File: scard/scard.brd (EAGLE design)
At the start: 47 x 86.5 mm, 66 parts, among them Q1 FDN360P, X1 COAX, X2 1365-20

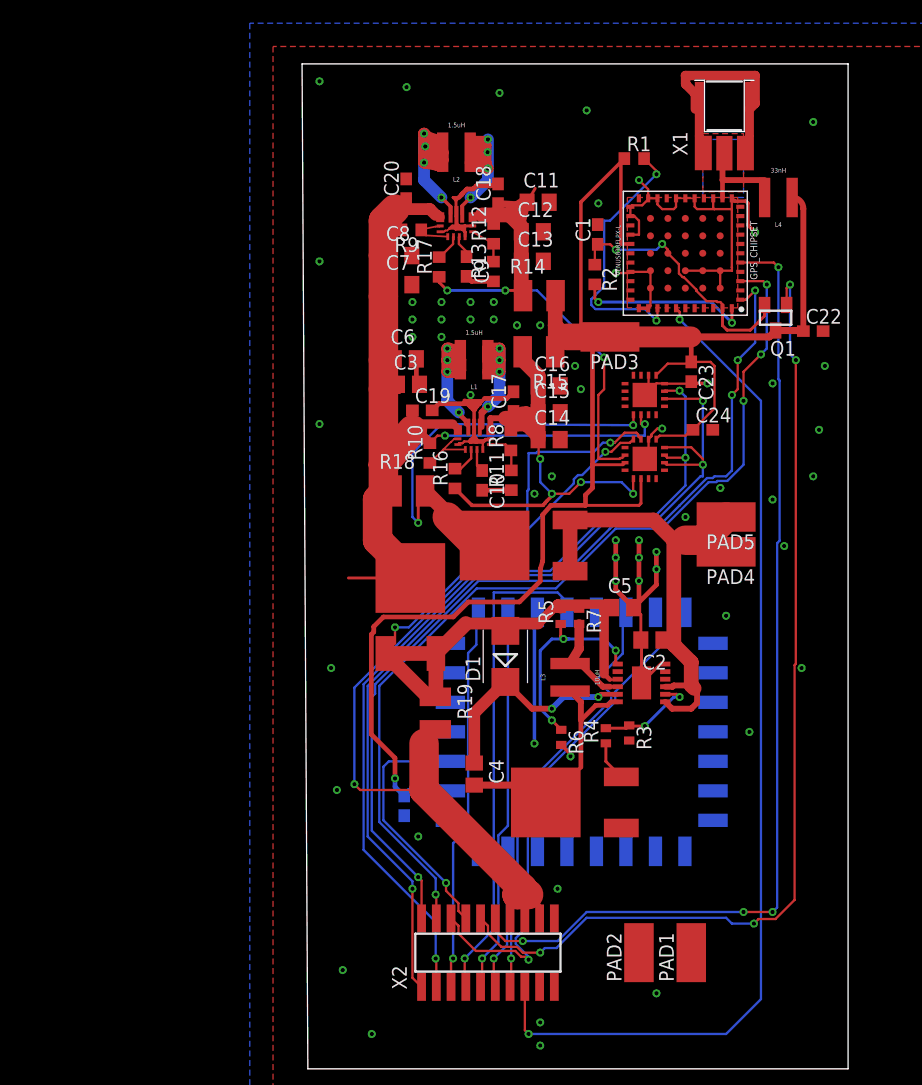
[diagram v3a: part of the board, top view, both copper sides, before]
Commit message: need switching voltage regulator capable of up to 8A
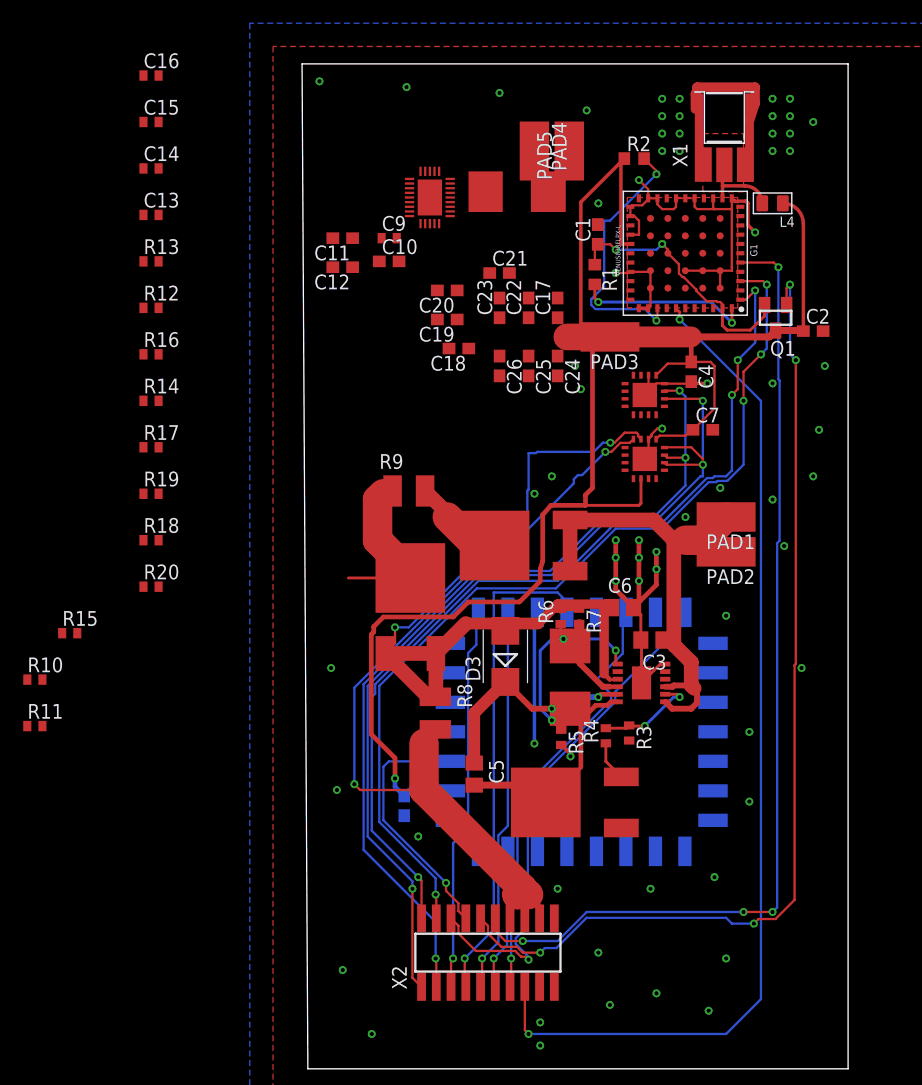
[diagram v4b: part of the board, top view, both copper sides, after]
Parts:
- removed L1: 1.5uH, calsat:XFL4020
- removed U$1: B085BM30, calsat:TO-252
- removed U$6, U$7: TPS63070, calsat:VQFN15
- added C25, C26: 10uF, resistor:C0603
- added D3: ES2D, diode:SMB
- added P1: TPS548A20, calsat:R-PWQFN-N28
- added R20: 3, rcl:R0402
- C10: value 100nF -> 10uF; device rcl:C0603 -> resistor:C0603
- C11, C12: value 22uF -> 10uF; device rcl:C0805 -> resistor:C0603
- C13: value 22uF -> 0.1uF; device rcl:C0805 -> resistor:C0402
- C14, C15: value 22uF -> 1uF; device rcl:C0805 -> resistor:C0402
- C16: value 22uF -> 470pF; device rcl:C0805 -> resistor:C0402
- C17, C18, C19, C20: value 10uF -> 22uF; device rcl:C0603 -> resistor:C0603
- C2: value 20uF -> 10uF; device resistor:C0805 -> resistor:C0603
- C21, C22: value 10uF -> 22uF
- C23, C24: value 0.1uF -> 10uF
- C3: value 10uF -> 20uF; device rcl:C0805 -> resistor:C0805
- C4: value 1uF -> 0.1uF; device resistor:C0805 -> resistor:C0603
- C5: value 10uF -> 1uF
- C6: device rcl:C0805 -> resistor:C0805
- C7: value 10uF -> 0.1uF; device rcl:C0805 -> resistor:C0603
- C8: device rcl:C0805 -> resistor:C0603
- C9: value 100nF -> 2.2nF; device rcl:C0603 -> resistor:C0402
- D1: value ES2D -> B085BM30; device diode:SMB -> calsat:TO-252
- L2: value 1.5uH -> 10uH; device calsat:XFL4020 -> calsat:SRP7028A
- L3: value 10uH -> 1.5uH; device calsat:XFL4020 -> calsat:SRP7028A
- L4: device calsat:XFL4020 -> Seeed-Inductor:L0805
- R1: value 1K -> 10K
- R10: value 10k -> 200k; device resistor:R0603 -> rcl:R0402
- R11: value 150k -> 200k; device resistor:R0603 -> rcl:R0402
- R12: value 470k -> 249k; device resistor:R0603 -> rcl:R0402
- R13: value 150k -> 105k; device resistor:R0603 -> rcl:R0402
- R14: value 0.01 -> 100k; device resistor:R1210 -> rcl:R0402
- R15: value 0.01 -> 0; device resistor:R1210 -> rcl:R0402
- R16: value 100k -> 150k; device resistor:R0603 -> rcl:R0402
- R17: value 100k -> 64.9k; device resistor:R0603 -> rcl:R0402
- R18: value 0.01 -> 9k; device resistor:R1210 -> rcl:R0402
- R19: value 0.01 -> 2k; device resistor:R1210 -> rcl:R0402
- R2: value 10K -> 1K
- R5: value ~630k -> ~410k
- R6: value ~410k -> ~630k
- R8: value 470k -> 0.01; device resistor:R0603 -> resistor:R1210
- R9: value 10k -> 0.01; device resistor:R0603 -> resistor:R1210
- moved C8 47.4 mm to (8.29, 22.6), flipped to the bottom, turned to 270 degrees
- moved R15 47.1 mm to (-20.5, 37.5), turned to 0 degrees
- moved C21 46.6 mm to (16.5, 68.5), flipped to the top, turned to 0 degrees
- moved L2 46.2 mm to (22.6, 33.7), turned to 90 degrees
- moved R11 46.1 mm to (-23.5, 29.5), turned to 0 degrees
- moved C16 43.5 mm to (-13.5, 85.5)
- moved C15 42.4 mm to (-13.5, 81.5)
- moved L3 42.0 mm to (18.0, 75.5), turned to 0 degrees
- moved C14 41.5 mm to (-13.5, 77.5)
- moved C4 39.3 mm to (33.0, 60.0)
- moved R10 39.2 mm to (-23.5, 33.5), turned to 0 degrees
- moved PAD4 38.2 mm to (19.5, 79.0), turned to 180 degrees
- moved PAD1 37.6 mm to (36.0, 47.5), turned to 90 degrees
- moved PAD2 35.3 mm to (36.0, 44.5), turned to 90 degrees
- moved R14 34.6 mm to (-13.5, 57.5)
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- renumbered A3 to A2, CHRG_IC to T1, GPS_CHIPSET to G1, U$2 to V1, U$4 to D4, U$5 to D2
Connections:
- net N$32 renamed SOLAR1_CUR
- net N$33 renamed VSOLAR1
- net N$34 renamed SOLAR2_CUR
- net N$35 renamed VSOLAR2
- removed net REG0_EN: R10.1, U$6.1, U$6.14
- removed net REG0_PGOOD: R16.2, U$6.2
- removed net REG1_3V3: A1.15, C11.1, C12.1, C13.1, C18.1, R12.2, R14.1, R17.1, U$7.7
- removed net REG1_EN: R9.1, U$7.1, U$7.14
- removed net REG1_PGOOD: R17.2, U$7.2
- removed net SYS_UNREG: A2.11, C19.1, C20.1, C3.1, C6.1, C7.1, C8.1, D4.1, R10.2, R18.1, R9.2, U$6.12, U$7.12
- new net N$1: P1.21, R16.1
- new net N$17: C16.1, R20.1
- new net N$2: C13.2, L3.1, P1.6, P1.7, P1.8, P1.9, R20.2
- new net SOLAR0_CUR: A2.12
- new net VSOLAR0: A2.11
- new net VSYS_UNREG: A1.14, C10.1, C11.1, C12.1, C14.1, C9.1, D4.1, P1.15, P1.16, P1.17, P1.19, R10.2, R9.1
- net +12V: now also C3.1, D1.2, D1.3, PAD1.1, PAD2.1; no longer C2.1, PAD4.1, PAD5.1, U$1.2, U$1.3
- net +3V3: now also C17.1, C18.1, C19.1, C2.1, C20.1, C25.1, C26.1, C4.1, C7.1, C8.1, L3.2, P1.24, R18.2, R2.1; no longer A1.14, R1.1, R14.2, R15.1
- net GND: now also C25.2, C26.2, C4.2, P1.10, P1.11, P1.12, P1.13, P1.14, P1.22, P1.27, P1.28, P1.29, PAD4.1, PAD5.1, R17.2, R19.1, R5.2; no longer C13.2, C5.2, PAD1.1, PAD2.1, R6.2, U$6.10, U$6.15, U$6.4, U$6.6, U$7.10, U$7.15, U$7.4, U$7.6
- net N$10: now also C15.1, P1.20, R12.2, R14.1; no longer R12.1, R13.2, U$7.5
- net N$11: now also P1.1, R12.1, R13.2; no longer L2.2, U$7.11
- net N$12: now also P1.2, R14.2, R16.2; no longer L2.1, U$7.9
- net N$13: now also P1.25, R17.1; no longer L1.1, U$6.9
- net N$14: now also P1.23, R18.1, R19.2; no longer R11.2, R8.1, U$6.5
- net N$15: now also P1.3, R10.1, R11.2; no longer L1.2, U$6.11
- net N$22: now also R1.1; no longer R2.1
- net N$3: now also C5.1, D3.C; no longer C4.1, D1.C
- net N$4: now also C5.2, L2.1; no longer C4.2, L3.1
- net N$5: now also P1.4, R15.1; no longer C9.1, U$7.3
- net N$6: now also L2.2; no longer L3.2
- net N$7: now also R2.2; no longer R1.2
- net N$8: now also R1.2; no longer R2.2
- net N$9: now also C13.1, R15.2; no longer C10.1, U$6.3
- net REG0_3V3: no longer C14.1, C15.1, C16.1, C17.1, R15.2, R16.1, R8.2, U$6.7
- net SYS_UNREG_CUR: now also A1.15, D1.1, R9.2; no longer A2.12, R18.2, U$1.1
- net VBATT: now also R8.2; no longer R19.2
- net VBATT_CUR: now also C6.1, D3.A, R6.2, R8.1; no longer C5.1, D1.A, R19.1, R5.2
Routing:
- net SYS_UNREG: track 86.0 -> 0.00 mm, vias 2 -> 0
- net REG1_3V3: track 52.2 -> 0.00 mm, vias 3 -> 0
- net REG0_3V3: track 50.1 -> 0.00 mm, vias 4 -> 0
- net GND: track 159.1 -> 118.0 mm, vias 60 -> 68
- net SYS_UNREG_CUR: track 38.2 -> 8.12 mm, vias 2 -> 0
- net N$11: track 26.0 -> 0.00 mm, vias 4 -> 0
- net N$12: track 21.3 -> 0.00 mm, vias 4 -> 0
- net VSYS_UNREG: track 0.00 -> 15.6 mm
- net N$15: track 14.9 -> 0.00 mm, vias 4 -> 0
- net N$13: track 13.6 -> 0.00 mm, vias 4 -> 0
- net +3V3: track 152.0 -> 142.7 mm
- net REG0_EN: track 5.17 -> 0.00 mm
- net REG1_EN: track 4.29 -> 0.00 mm
- net N$14: track 3.77 -> 0.00 mm
- net N$10: track 3.65 -> 0.00 mm
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- removed copper zone on layer 16, net NONE

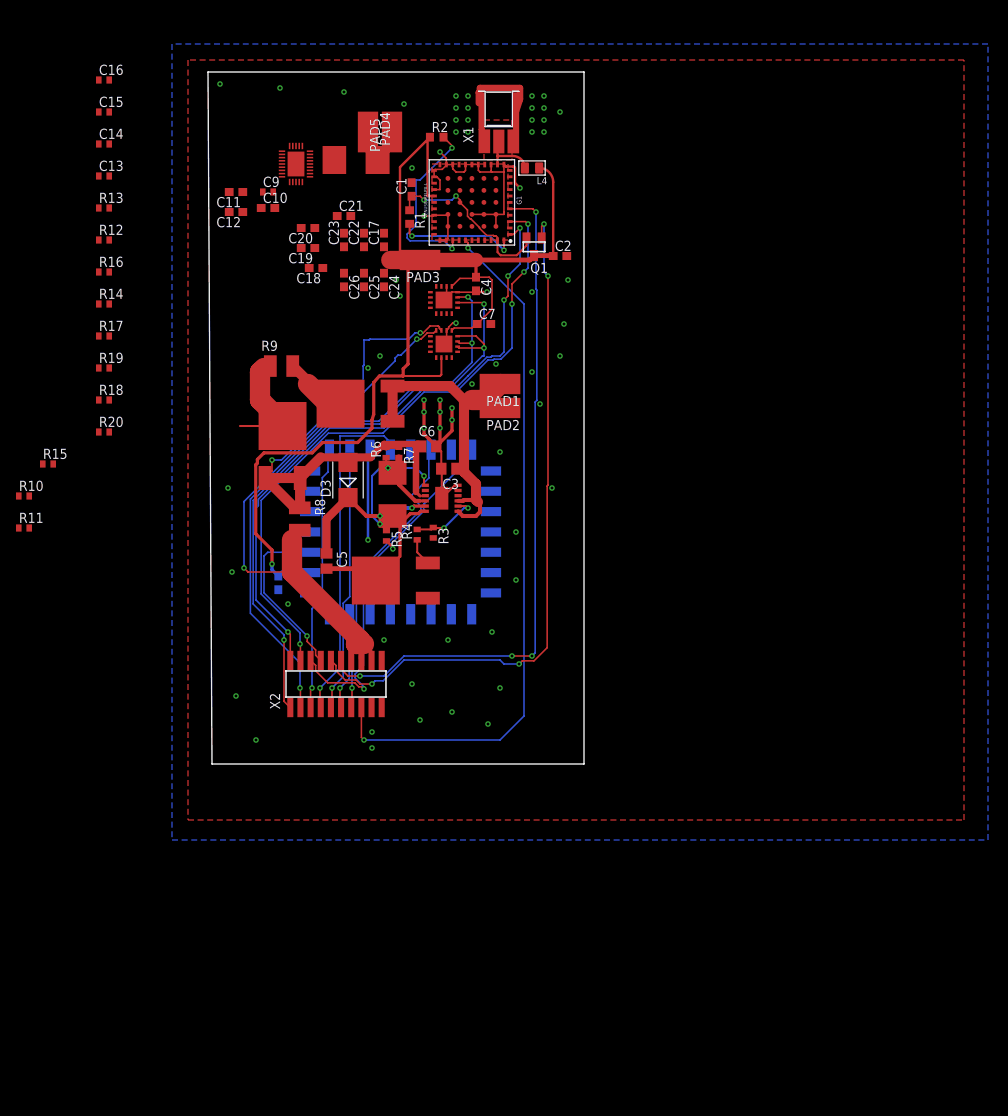
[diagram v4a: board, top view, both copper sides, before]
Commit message: Andrea's changes, including routing power supply components, gps thermal vias, and more capacitors
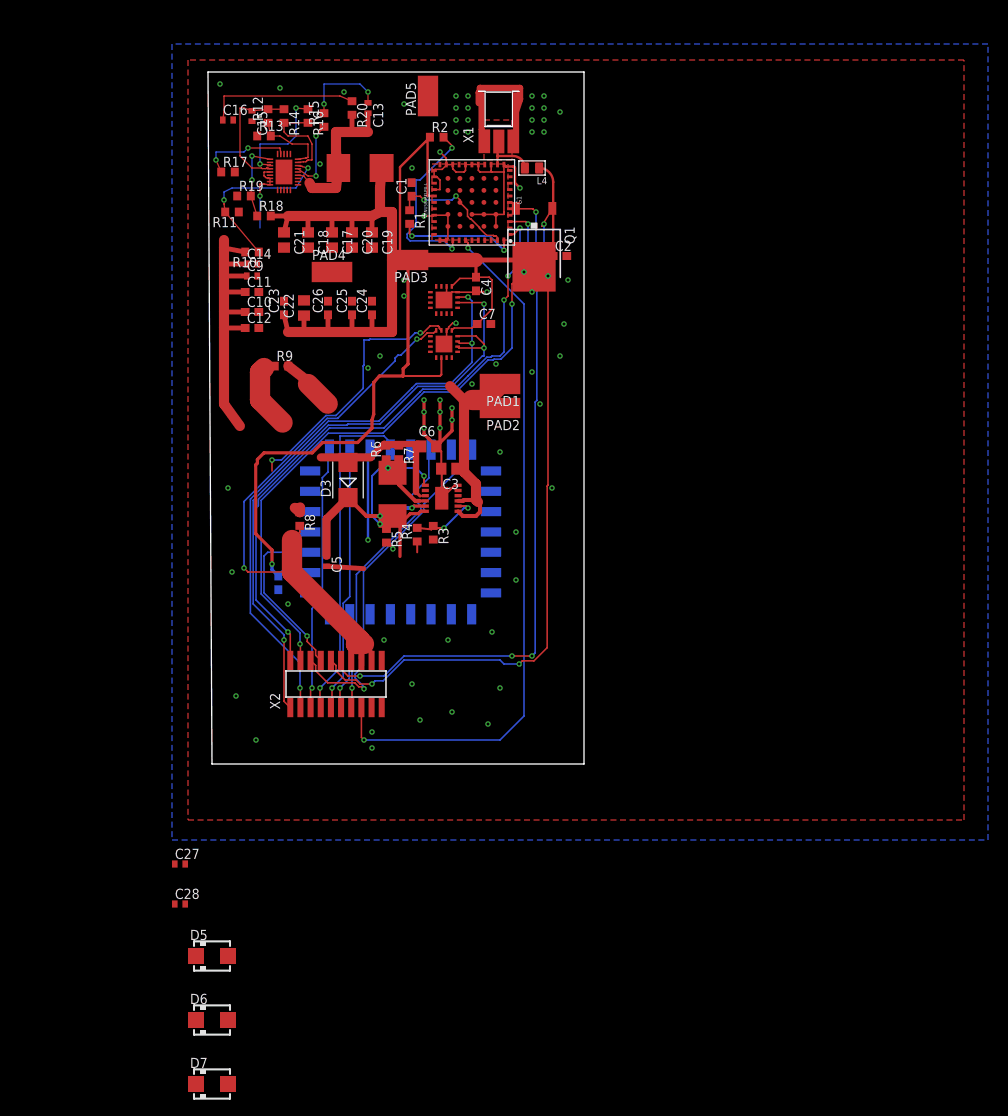
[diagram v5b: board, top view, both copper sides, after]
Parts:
- removed D1, D2, D4: B085BM30, calsat:TO-252
- added C27: 1uF, resistor:C0402
- added C28: 470pF, resistor:C0402
- added D5, D6, D7: MBRA340T3, diode:SMA
- C17, C18, C19, C20, C21, C22: device resistor:C0603 -> rcl:C0805
- C3: value 20uF -> 22uF
- C5: device resistor:C0805 -> rcl:C0402
- Q1: value FDN360P -> FDD4141TO252; device transistor-power:SUPER-SOT3 -> transistor-fet:TO252
- R1: device resistor:R0603 -> rcl:R0603
- R10, R11, R12, R15, R16, R17, R18, R19, R20: device rcl:R0402 -> rcl:R0603
- R13: value 105k -> 100k; device rcl:R0402 -> rcl:R0603
- R14: value 100k -> 412k; device rcl:R0402 -> rcl:R0603
- R3: value (none) -> 412k; device resistor:R0402 -> rcl:R0603
- R4: value (none) -> 100k; device resistor:R0402 -> rcl:R0603
- R5: value ~410k -> 412k; device resistor:R0402 -> rcl:R0603
- R6: value ~630k -> 634k; device resistor:R0402 -> rcl:R0603
- R7: device resistor:R0402 -> rcl:R0603
- R8, R9: device resistor:R1210 -> rcl:R0603
- moved R15 55.1 mm to (14.0, 80.5), turned to 90 degrees
- moved R20 51.0 mm to (17.5, 82.0), turned to 270 degrees
- moved R11 47.3 mm to (2.50, 69.0), turned to 180 degrees
- moved R10 41.7 mm to (5.00, 64.0), turned to 180 degrees
- moved C13 34.1 mm to (19.5, 82.0), turned to 270 degrees
- moved R14 32.5 mm to (9.00, 81.0), turned to 270 degrees
- moved R16 32.1 mm to (12.0, 81.0), turned to 270 degrees
- moved R18 30.5 mm to (6.50, 68.5)
- moved R19 27.7 mm to (4.00, 71.0)
- moved R12 25.7 mm to (7.00, 81.0), turned to 90 degrees
- moved R17 25.7 mm to (2.00, 74.0)
- moved C14 23.8 mm to (5.00, 62.5)
- moved R13 21.9 mm to (6.50, 78.5)
- moved C15 18.5 mm to (5.00, 81.0), turned to 270 degrees
- moved PAD4 18.1 mm to (15.0, 61.5), turned to 270 degrees
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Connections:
- removed net N$22: C1.1, G1.2, G1.58, Q1.2, R1.1
- removed net V_SOLAR_UNREG: R3.2
- new net N$16: C1.1, G1.2, G1.58, Q1.3, R1.1
- net +12V: now also D5.A, R3.2; no longer D1.2, D1.3
- net +3V3: now also C27.1, C28.1, Q1.2; no longer Q1.3
- net GND: now also C27.2, C28.2, D7.A; no longer D2.2, D2.3
- net N$4: now also D7.C; no longer D2.1
- net SYS_UNREG_CUR: now also D5.C; no longer D1.1
- net VBATT_CUR: now also D6.A; no longer D4.2, D4.3
- net VSYS_UNREG: now also D6.C; no longer D4.1
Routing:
- net +3V3: track 142.7 -> 209.0 mm
- net VSYS_UNREG: track 15.6 -> 60.2 mm, vias 0 -> 1
- net N$22: track 22.9 -> 0.00 mm, vias 2 -> 0
- net N$15: track 0.00 -> 22.4 mm, vias 0 -> 2
- net N$2: track 0.00 -> 21.1 mm
- net N$17: track 0.00 -> 19.1 mm
- net VBATT_CUR: track 75.9 -> 58.5 mm
- net N$10: track 0.00 -> 16.0 mm
- net N$16: track 0.00 -> 15.8 mm, vias 0 -> 2
- net N$1: track 0.00 -> 13.8 mm, vias 0 -> 2
- net N$12: track 0.00 -> 12.3 mm
- net N$13: track 0.00 -> 11.6 mm, vias 0 -> 2
- net +12V: track 43.2 -> 31.6 mm
- net N$9: track 0.00 -> 10.9 mm, vias 0 -> 2
- net N$14: track 0.00 -> 9.92 mm, vias 0 -> 2
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
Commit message: final DRC fixes
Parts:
- added R21: 0.01, rcl:R0603
- Q1: value FDD4141TO252 -> FDN360P; device transistor-fet:TO252 -> transistor-power:SUPER-SOT3
- moved C28 90.2 mm to (40.5, 61.0), turned to 270 degrees
- moved C27 86.7 mm to (42.0, 61.0), turned to 270 degrees
- moved D6 74.2 mm to (10.5, 41.5), turned to 270 degrees
- moved D5 72.4 mm to (18.5, 46.0)
- moved D7 66.4 mm to (22.5, 22.5), turned to 270 degrees
- moved C16 17.9 mm to (19.2, 75.5), turned to 90 degrees
- moved R5 15.5 mm to (24.5, 43.8), turned to 0 degrees
- moved C23 13.0 mm to (22.0, 57.5), flipped to the bottom, turned to 270 degrees
- moved R18 13.0 mm to (19.0, 65.0)
- moved R19 13.0 mm to (15.5, 65.0)
- moved C21 12.0 mm to (18.0, 57.5), turned to 180 degrees
- moved C12 11.7 mm to (3.00, 66.0), turned to 180 degrees
- moved C18 8.14 mm to (18.0, 60.0), turned to 180 degrees
- moved R17 8.14 mm to (10.0, 75.5), turned to 90 degrees
- moved R12 7.83 mm to (3.50, 74.0), turned to 0 degrees
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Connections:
- net +3V3: now also R21.1; no longer L3.2
- net REG0_3V3: now also L3.2, R21.2
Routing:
- net +3V3: track 209.0 -> 243.4 mm, vias 1 -> 16
- net REG0_3V3: track 0.00 -> 24.8 mm, vias 0 -> 2
- net GND: track 115.8 -> 136.3 mm, vias 68 -> 102
- net N$17: track 19.1 -> 2.32 mm
- net +12V: track 31.6 -> 48.2 mm
- net SYS_UNREG_CUR: track 6.92 -> 22.5 mm, vias 0 -> 2
- net N$14: track 9.92 -> 22.0 mm
- net N$13: track 11.6 -> 2.48 mm, vias 2 -> 0
- net N$9: track 10.9 -> 1.80 mm, vias 2 -> 0
- net N$16: track 15.8 -> 24.3 mm
- net N$11: track 9.59 -> 17.6 mm, vias 0 -> 2
- net N$4: track 15.2 -> 22.3 mm
- net VSYS_UNREG: track 60.2 -> 66.9 mm, vias 1 -> 0
- net N$15: track 22.4 -> 15.8 mm
- net N$2: track 21.1 -> 14.5 mm
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- removed copper zone on layer 1, net NONE2
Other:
- outline, holes or cut-outs redrawn
